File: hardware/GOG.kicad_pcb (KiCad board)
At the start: 2 copper layers, 118 x 64 mm, 133 parts, among them J1 USB_C_Receptacle_USB2.0_16P, J10 Conn_01x04, J11 Conn_01x02, J2 Conn_01x02_Pin, J3 Conn_01x04_Pin, J4 Conn_01x02_Pin, J5 85201239, J6 Conn_01x04_Pin, J7 Conn_01x04_Pin, J8 Screw_Terminal_01x02, J9 Conn_01x02, Q1 Q_PMOS, Q2 Q_NMOS, Q3 Q_NMOS, Q4 Q_NMOS, Q5 Q_NMOS, SW1 SW_Omron_B3FS, SW2 SW_Omron_B3FS, U1 ESP32-C3-WROOM-02, U2 USBLC6-2SC6, U3 RFM95W-868S2, U4 SAM-M8Q, U5 BQ25798RQMR, U6 AP63203WU, U7 AP63205WU

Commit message: Finished battery manager placement
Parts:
- removed the R15 at (243.7, 154.0)
- removed the TP1 at (254.3, 155.7)
- removed the TP11 at (238.2, 123.3)
- removed the TP16 at (241.8, 116.2)
- removed the TP19 at (241.8, 126.8)
- removed the TP23 at (245.3, 116.2)
- C15, C20, C28, C8, C9: footprint Capacitor_SMD:C_0402_1005Metric -> GoG_Library:C_0402_1005Metric_JLCPCB
- C16, C19: footprint Capacitor_SMD:C_0603_1608Metric -> GoG_Library:C_0402_1005Metric_JLCPCB; moved to B.Cu
- C18: footprint Capacitor_SMD:C_0402_1005Metric -> GoG_Library:C_0402_1005Metric_JLCPCB; moved to B.Cu
- R16: renamed from R17; footprint Resistor_SMD:R_0402_1005Metric -> GoG_Library:R_0402_1005Metric_JLCPCB
- R18: renamed from R19; footprint Resistor_SMD:R_0402_1005Metric -> GoG_Library:R_0402_1005Metric_JLCPCB
- R19: renamed from R20; footprint Resistor_SMD:R_0402_1005Metric -> GoG_Library:R_0402_1005Metric_JLCPCB
- R20: renamed from R21; footprint Resistor_SMD:R_0402_1005Metric -> GoG_Library:R_0402_1005Metric_JLCPCB
- R21: renamed from R22; footprint Resistor_SMD:R_0402_1005Metric -> GoG_Library:R_0402_1005Metric_JLCPCB
- R22: renamed from R23; footprint Resistor_SMD:R_0402_1005Metric -> GoG_Library:R_0402_1005Metric_JLCPCB
- R23: renamed from R24; footprint Resistor_SMD:R_0402_1005Metric -> GoG_Library:R_0402_1005Metric_JLCPCB
- R24: renamed from R25; footprint Resistor_SMD:R_0402_1005Metric -> GoG_Library:R_0402_1005Metric_JLCPCB
- R25: renamed from R26; footprint Resistor_SMD:R_0402_1005Metric -> GoG_Library:R_0402_1005Metric_JLCPCB
- U3: footprint RF_Module:HOPERF_RFM9XW_SMD -> GoG_Library:HOPERF_RFM9XW_SMD
- moved J10 128.0 mm to (162.9, 148.8), turned to 90 degrees
- moved L1 91.3 mm to (177.2, 125.5), turned to 90 degrees
- moved J11 80.3 mm to (212.8, 95.3), turned to 180 degrees
- moved D5 80.1 mm to (190.2, 144.4)
- moved C16 78.4 mm to (184.9, 127.5), turned to 180 degrees
- moved TH1 77.6 mm to (190.9, 123.6)
- moved C19 77.5 mm to (184.9, 123.5), turned to 180 degrees
- moved D4 76.3 mm to (195.2, 144.4)
- moved R17 73.5 mm to (189.0, 133.2), turned to 90 degrees
- moved C25 73.3 mm to (181.2, 111.7), turned to 180 degrees
- moved C24 72.8 mm to (181.2, 114.0), turned to 180 degrees
- moved C23 72.6 mm to (181.2, 116.2), turned to 180 degrees
- moved C17 72.0 mm to (190.5, 121.6)
- moved C10 70.7 mm to (181.2, 134.7), turned to 180 degrees
- moved C22 69.9 mm to (181.2, 118.5), turned to 180 degrees
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- renumbered R16 to R15, R18 to R17, TP2 to TP1, TP12 to TP10, TP13 to TP11, TP14 to TP12, TP15 to TP13, TP17 to TP14, TP18 to TP15, TP20 to TP16, TP21 to TP17, TP22 to TP18, TP24 to TP19, TP3 to TP2, TP25 to TP20, TP26 to TP21, TP27 to TP22, TP28 to TP23, TP29 to TP24, TP4 to TP3, TP5 to TP4, TP6 to TP5, TP7 to TP6, TP8 to TP7, TP9 to TP8, TP10 to TP9
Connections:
- Q1 pad 3: Net-(Q1-D) -> VSOL
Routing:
- net Net-(U5-SW2): vias 0 -> 1
- net Net-(U5-SW1): vias 0 -> 1
- net GND: vias 0 -> 4
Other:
- board size 118 x 64 mm -> 118 x 70.2 mm
- board text added: "GND"
- board text added: "RX"
- board text added: "SCL"
- board text added: "SDA"
- board text added: "TX"
- board text added: "VBAT"
- board text added: "VSOL"
- board text added: "~{CE}"
- board text added: "~{INT}"

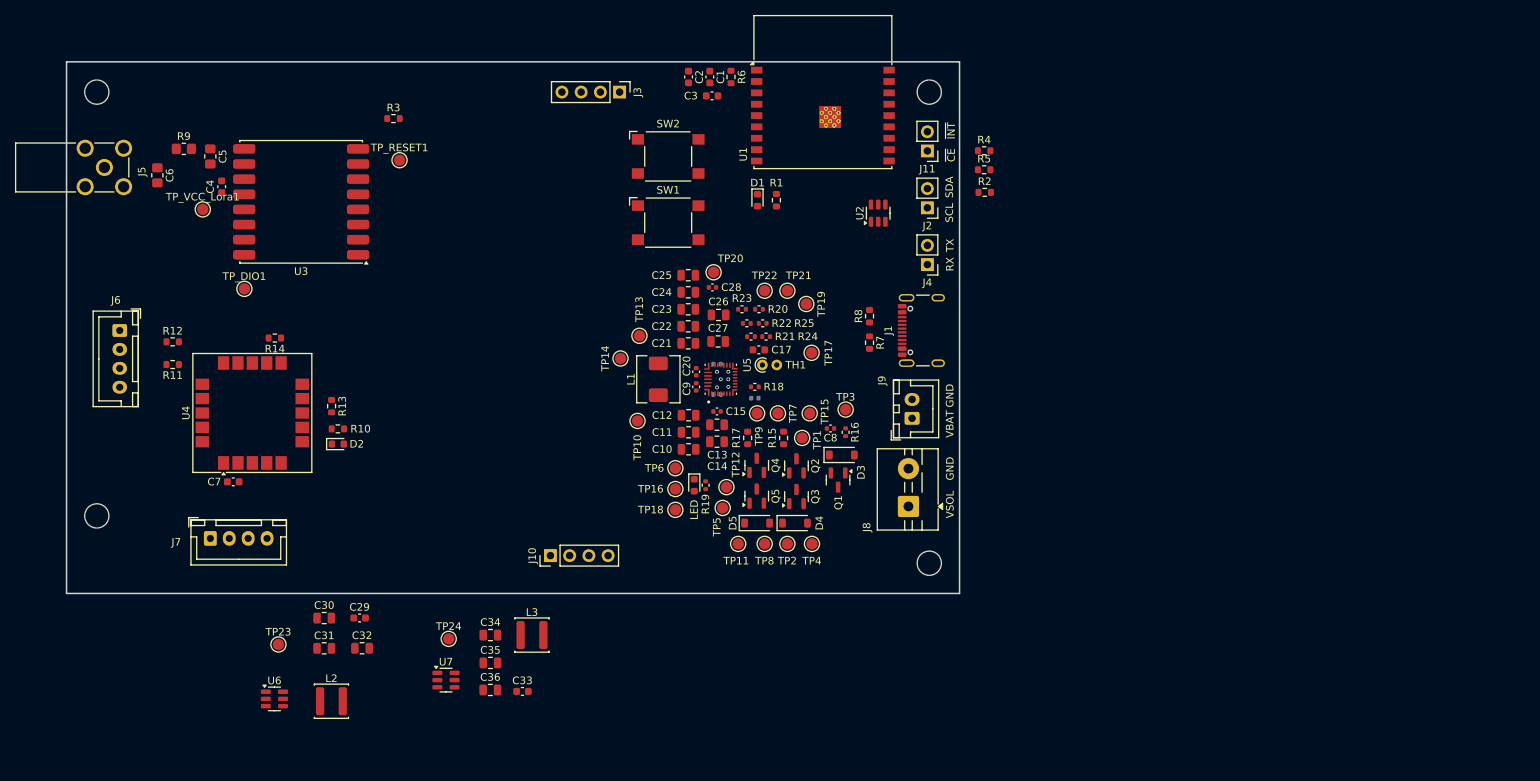
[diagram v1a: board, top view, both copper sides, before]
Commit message: Finished optimal placement & adapted/fixed schematic
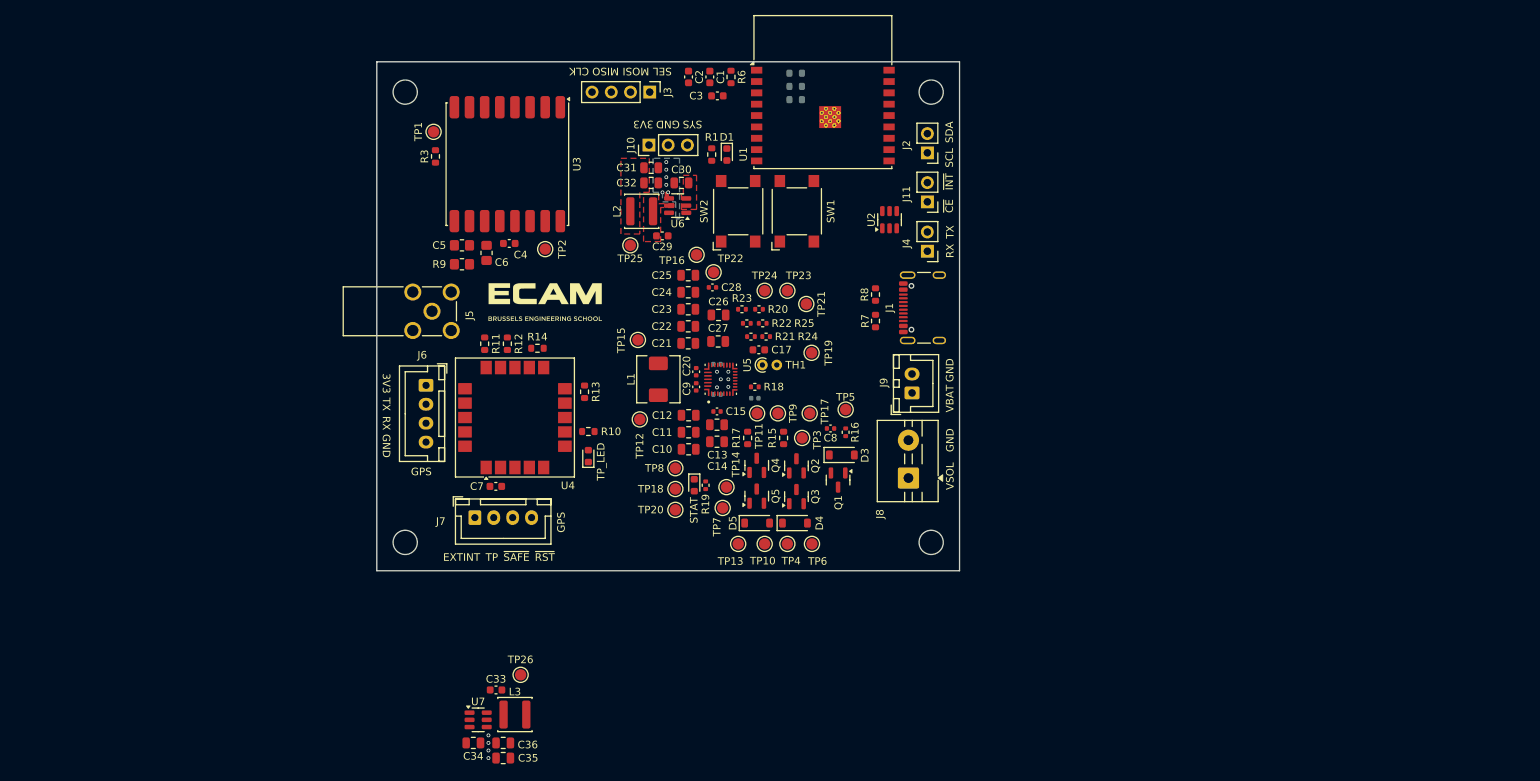
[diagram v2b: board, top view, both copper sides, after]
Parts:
- removed TP_VCC_Lora1: TestPoint, GoG_Library:TestPoint_Pad_D1.5mm_JLCPCB
- added G***: LOGO, GoG_Library:ECAM_logo, F.Cu at (162.2, 114.1)
- J10: value Conn_01x04 -> Conn_01x03; footprint Connector_PinHeader_2.54mm:PinHeader_1x04_P2.54mm_Vertical -> Connector_PinHeader_2.54mm:PinHeader_1x03_P2.54mm_Vertical
- R2, R4, R5: moved to B.Cu
- moved U6 84.2 mm to (179.8, 102.5), turned to 180 degrees
- moved C31 76.8 mm to (176.2, 97.5)
- moved L2 76.6 mm to (175.0, 103.2), turned to 180 degrees
- moved C30 74.4 mm to (180.2, 99.5), turned to 180 degrees
- moved C32 72.4 mm to (176.2, 99.5)
- moved TP25 70.3 mm to (173.5, 107.8), turned to 180 degrees
- moved C29 64.4 mm to (177.7, 106.5), turned to 180 degrees
- moved J10 55.8 mm to (176.0, 94.5)
- moved J5 47.3 mm to (147.3, 116.5)
- moved C6 44.7 mm to (154.5, 108.8), turned to 90 degrees
- moved R12 44.2 mm to (157.2, 120.8), turned to -90 degrees
- moved R11 41.3 mm to (154.2, 120.8), turned to 90 degrees
- moved J6 41.1 mm to (146.5, 126.2)
- moved REF** 40.9 mm to (143.8, 147.0)
- moved REF** 40.8 mm to (143.8, 87.5)
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- renumbered TP_RESET1 to TP1, TP8 to TP10, TP9 to TP11, TP10 to TP12, TP11 to TP13, TP12 to TP14, TP13 to TP15, TP14 to TP16, TP15 to TP17, TP16 to TP18, TP17 to TP19, TP_DIO1 to TP2, TP18 to TP20, TP19 to TP21, TP20 to TP22, TP21 to TP23, TP22 to TP24, TP23 to TP25, TP24 to TP26, TP1 to TP3, TP2 to TP4, TP3 to TP5, TP4 to TP6, TP5 to TP7, TP6 to TP8, TP7 to TP9
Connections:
- C29 pad 2: 3.3V -> Net-(U6-SW)
- C33 pad 2: 5V -> Net-(U7-SW)
- C4 pad 1: GND -> 3.3V
- C4 pad 2: 3.3V -> GND
- J10 pad 1: /Power/VSYS -> 3.3V
- J10 pad 2: 5V -> GND
- J10 pad 3: 3.3V -> /Power/VSYS
- J7 pad 2: TP -> ~{reset}
- J7 pad 4: ~{reset} -> TP
- J9 pad 1: /Power/VBAT -> GND
- J9 pad 2: GND -> /Power/VBAT
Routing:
- net GND: track 0.00 -> 1.01 mm, vias 4 -> 14
- added copper zone on F.Cu, net /Power/VSYS
- added copper zone on F.Cu, net 3.3V
- added copper zone on B.Cu, net GND
- added copper zone on F.Cu, net Net-(U6-SW)
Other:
- board size 118 x 70.2 mm -> 77 x 67.2 mm
- board text added: "3V3"
- board text added: "CLK"
- board text added: "EXTINT"
- board text added: "GPS"
- board text added: "MISO"
- board text added: "MOSI"
- board text added: "SEL"
- board text added: "STAT"
- board text added: "SYS"
- board text added: "TP"
- board text added: "TP_LED"
- board text added: "~{RST}"
- board text added: "~{SAFE}"

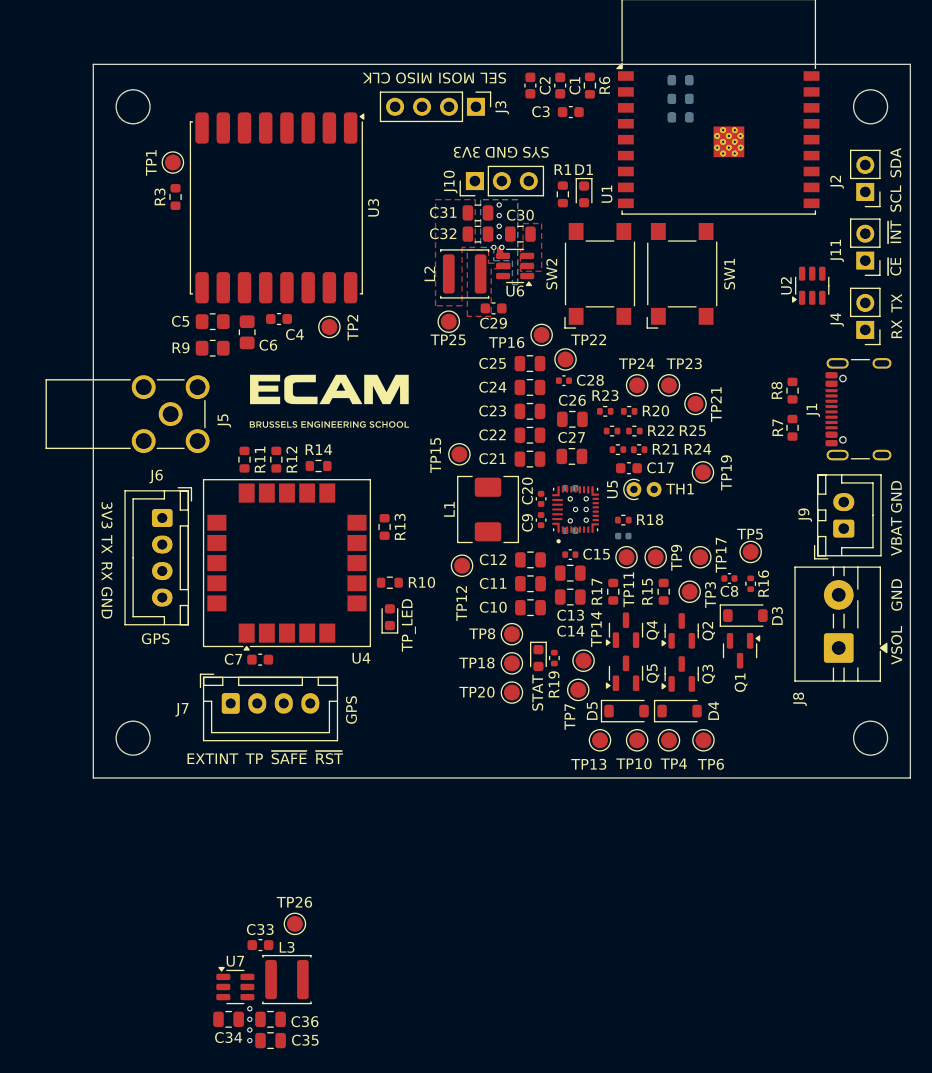
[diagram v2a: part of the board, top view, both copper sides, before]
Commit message: Finished PCB routing
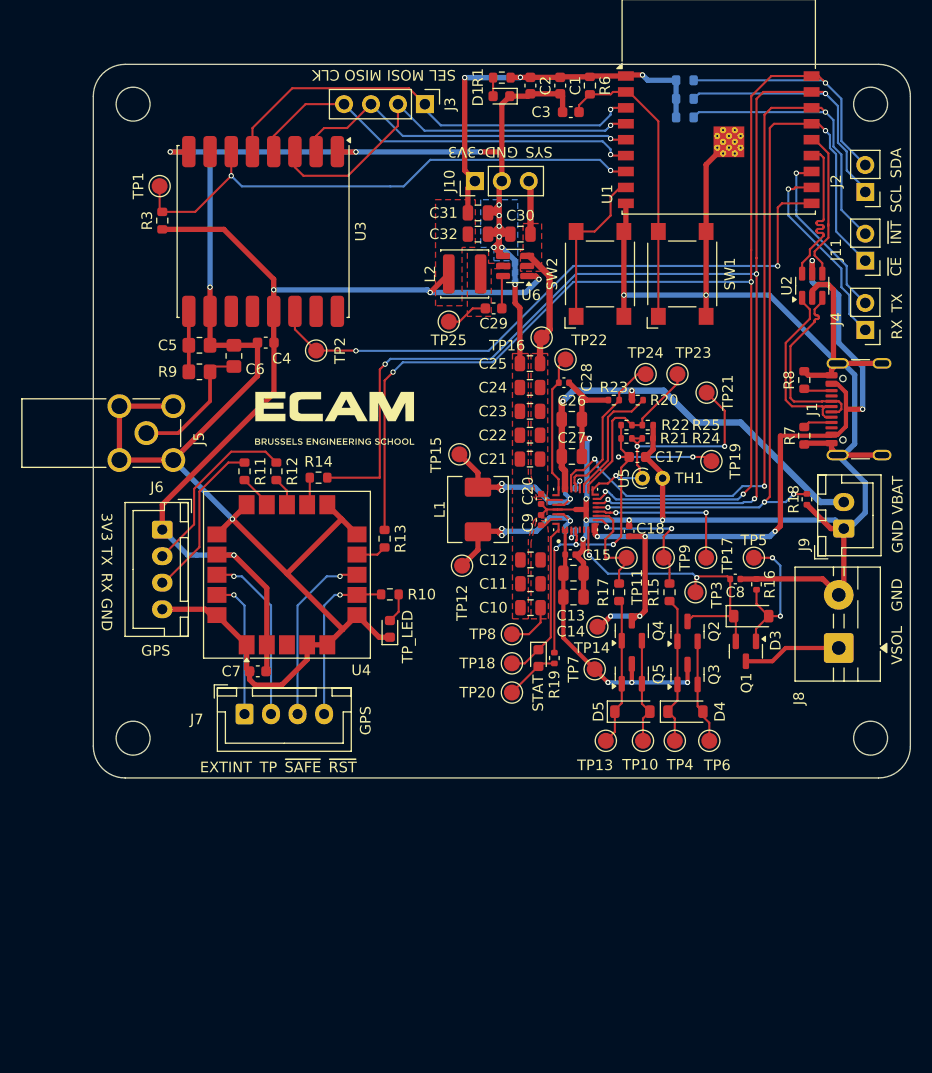
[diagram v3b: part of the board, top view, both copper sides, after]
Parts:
- removed C33: 0.1u, Capacitor_SMD:C_0603_1608Metric
- removed C34: 10u, Capacitor_SMD:C_0805_2012Metric
- removed C35, C36: 22u, Capacitor_SMD:C_0805_2012Metric
- removed L3: 4.7u, Inductor_SMD:L_Sunlord_SWPA4030S
- removed TP26: TestPoint, GoG_Library:TestPoint_Pad_D1.5mm_JLCPCB
- removed U7: AP63205WU, Package_TO_SOT_SMD:TSOT-23-6
- C18: moved to F.Cu
- moved R18 17.4 mm to (207.2, 124.5), turned to 90 degrees
- moved R1 12.4 mm to (178.5, 84.8), turned to 180 degrees
- moved D1 12.1 mm to (178.5, 86.5), turned to 180 degrees
- moved J3 4.82 mm to (171.2, 87.2)
- moved TP14 3.45 mm to (187.5, 136.5)
- moved J5 2.91 mm to (145.0, 118.2)
- moved C4 2.55 mm to (156.2, 109.7)
- moved C5 2.55 mm to (150.0, 110.0)
- moved C6 2.55 mm to (153.2, 111.0)
- moved R3 2.55 mm to (146.5, 98.2)
- moved R9 2.55 mm to (150.0, 112.5)
- moved TP1 2.55 mm to (146.2, 95.0)
- moved TP2 2.55 mm to (161.0, 110.5)
- moved U3 2.55 mm to (156.0, 99.2)
- moved TP7 2.49 mm to (187.2, 140.5)
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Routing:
- net GND: track 1.01 -> 384.9 mm, vias 14 -> 20
- net SCL: track 0.00 -> 137.9 mm, vias 0 -> 5
- net SDA: track 0.00 -> 135.0 mm, vias 0 -> 5
- net 3.3V: track 0.00 -> 129.5 mm, vias 0 -> 7
- net BQ_INT_N: track 0.00 -> 89.1 mm, vias 0 -> 3
- net BQ_CE_N: track 0.00 -> 75.4 mm, vias 0 -> 4
- net VBUS: track 0.00 -> 72.7 mm, vias 0 -> 7
- net RFM_DIO0: track 0.00 -> 60.2 mm, vias 0 -> 2
- net RFM_RESET: track 0.00 -> 51.8 mm, vias 0 -> 2
- net SPI_SELECT: track 0.00 -> 41.7 mm, vias 0 -> 1
- net /Power/VBAT: track 0.00 -> 41.0 mm, vias 0 -> 2
- net /Power/REGN: track 0.00 -> 39.0 mm, vias 0 -> 5
- net SPI_MOSI: track 0.00 -> 38.3 mm, vias 0 -> 1
- net SPI_CLK: track 0.00 -> 38.2 mm, vias 0 -> 1
- net SPI_MISO: track 0.00 -> 33.3 mm, vias 0 -> 1
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- added copper zone on F.Cu, net GND
- added copper zone on F.Cu, net Net-(U5-PMID)
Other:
- outline, holes or cut-outs redrawn

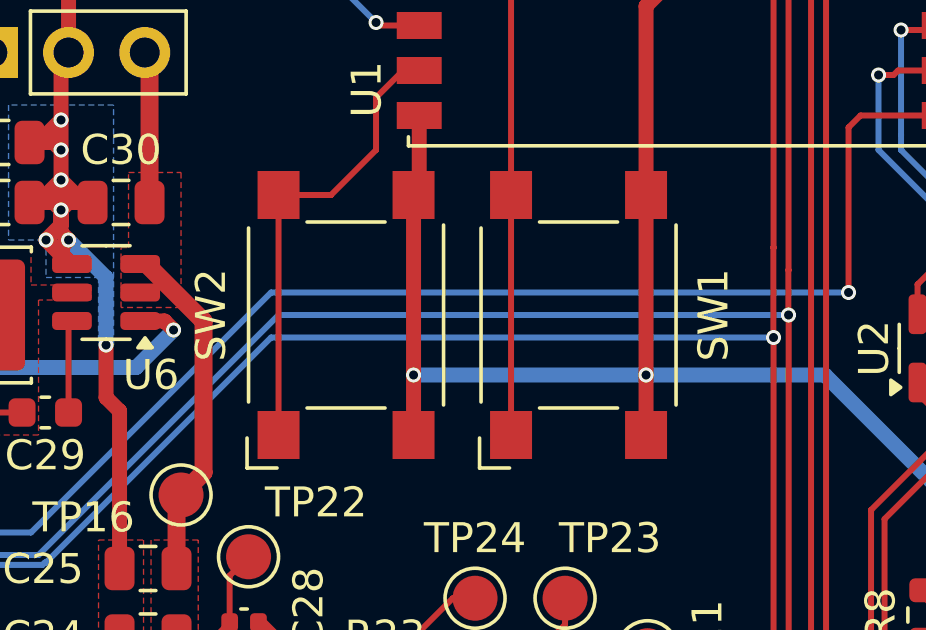
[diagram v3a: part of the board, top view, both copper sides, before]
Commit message: Find all remaining components on JLCPCB
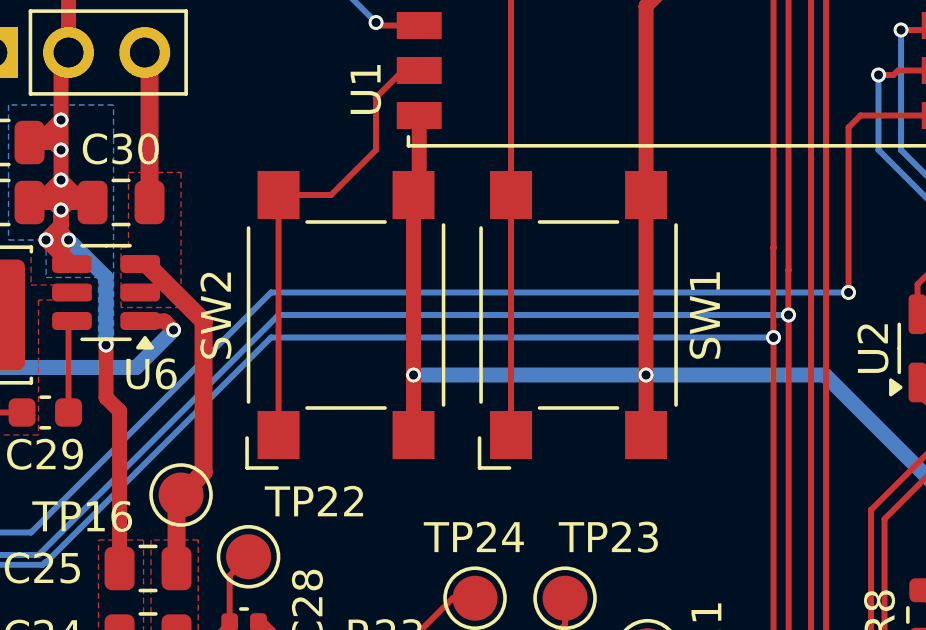
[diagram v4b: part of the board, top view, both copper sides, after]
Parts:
- C5, C6: value C -> (NC)
- SW1, SW2: footprint Button_Switch_SMD:SW_SPST_Omron_B3FS-100xP -> Button_Switch_SMD:SW_SPST_Omron_B3FS-101xP
